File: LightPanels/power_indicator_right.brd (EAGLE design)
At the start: 47.5 x 48 mm, 22 parts

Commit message: Latest light panel pcb files
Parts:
- moved U$7 36.3 mm to (9.05, 9.37), turned to 180 degrees
- moved C7 35.9 mm to (8.89, 13.0), turned to 0 degrees
- moved U$1 35.8 mm to (24.1, 37.1), turned to 270 degrees
- moved C1 34.7 mm to (21.0, 34.6), turned to 270 degrees
- moved U$2 25.6 mm to (22.2, 27.5), turned to 270 degrees
- moved PAD8 23.3 mm to (19.1, 20.3), turned to 90 degrees
- moved C2 23.0 mm to (20.6, 22.9), turned to 270 degrees
- moved PAD6 22.7 mm to (19.1, 8.89), turned to 90 degrees
- moved C6 22.1 mm to (18.7, 15.2), turned to 0 degrees
- moved PAD7 21.8 mm to (19.1, 16.5), turned to 90 degrees
- moved U$6 21.8 mm to (19.1, 11.7), turned to 180 degrees
- moved PAD5 21.6 mm to (19.1, 12.7), turned to 90 degrees
- moved C3 17.7 mm to (24.1, 21.3), turned to 90 degrees
- moved U$3 14.1 mm to (27.5, 21.3), turned to 270 degrees
- moved PAD4 12.7 mm to (27.9, 20.3), turned to 90 degrees
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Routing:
- net GND: track 36.5 -> 41.1 mm
- net +5V: track 6.69 -> 7.96 mm, vias 1 -> 2
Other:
- board size 47.5 x 48 mm -> 48 x 47.5 mm

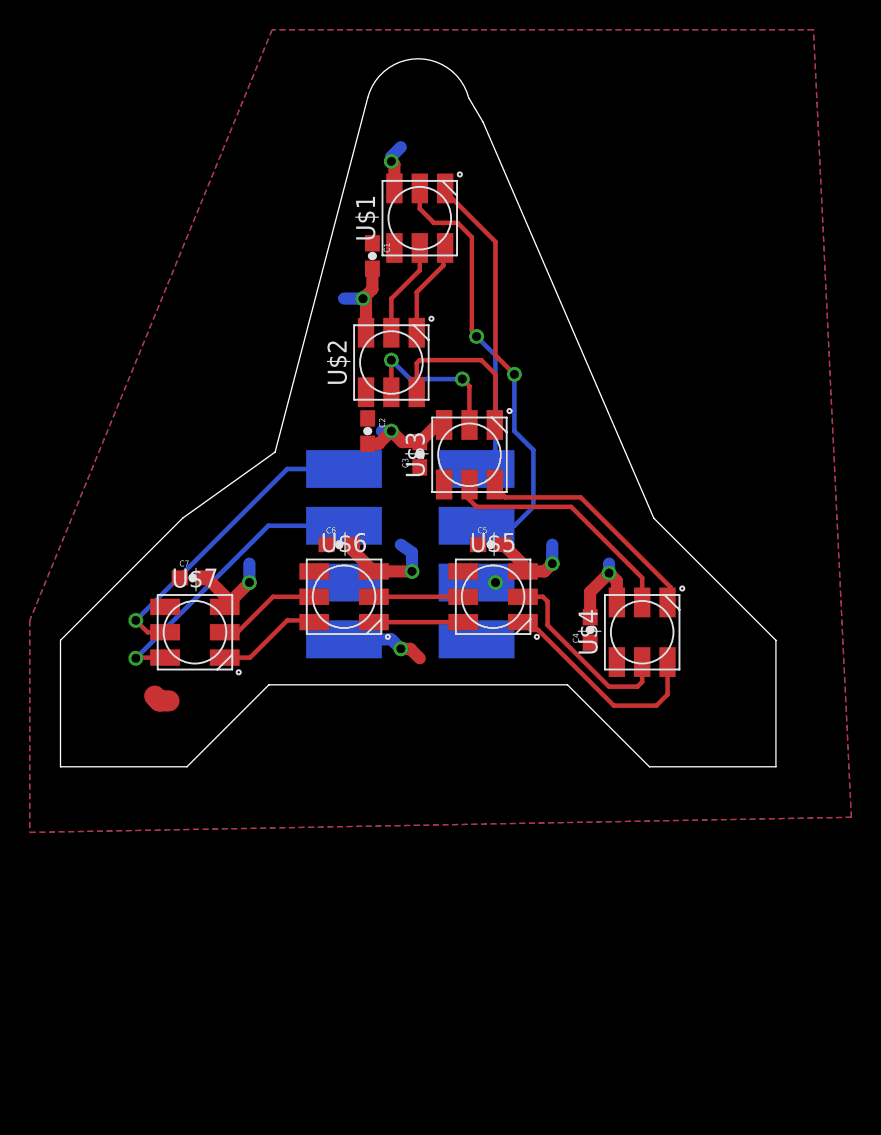
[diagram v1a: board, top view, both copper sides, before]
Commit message: Power indicators more or less done
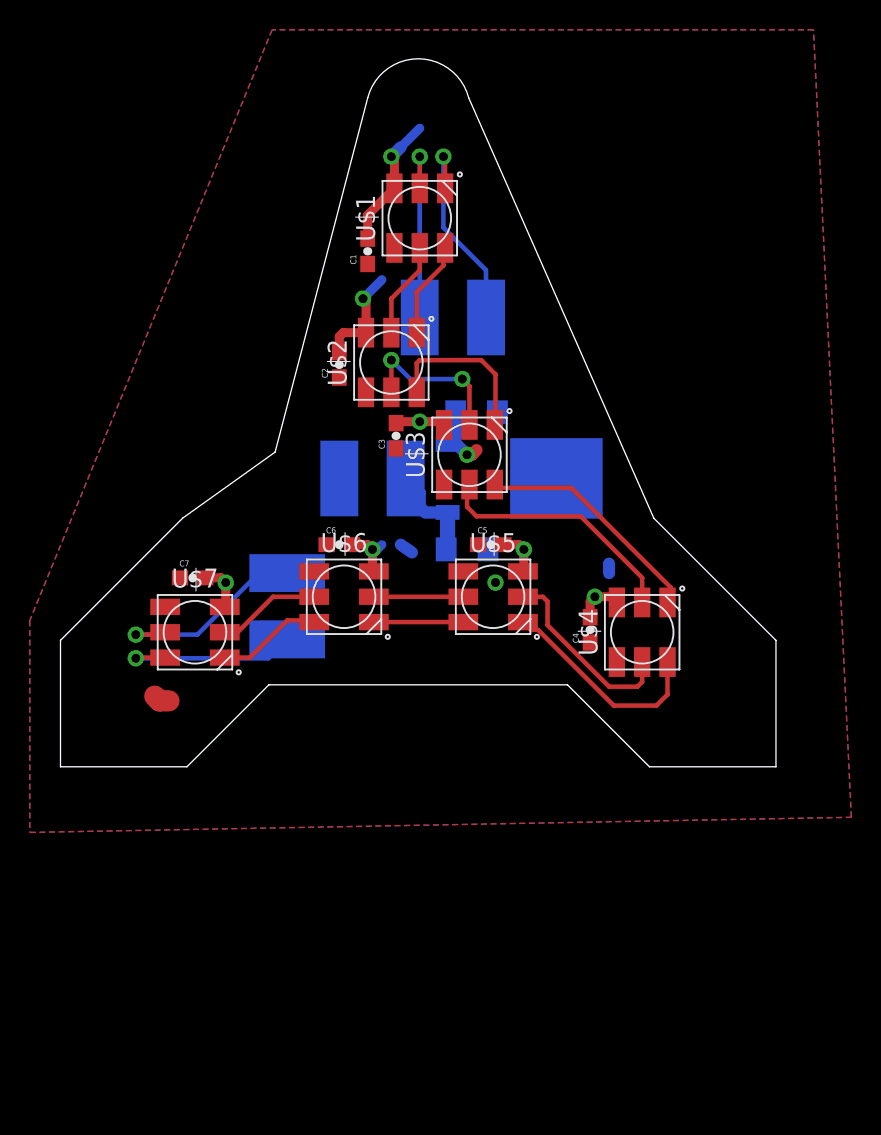
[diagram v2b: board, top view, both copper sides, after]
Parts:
- removed PAD1, PAD2, PAD3, PAD4, PAD5, PAD6, PAD7, PAD8: WIREPADSMD2,54-5,08, wirepad:SMD2,54-5,08
- added +12V, CI, CO, DI, DO, GND: WIREPADSMD2,54-5,08, wirepad:SMD2,54-5,08
- added C8, C9: 10uF, SparkFun-Retired:EIA3216
- added IC1: 7805DT, linear:TO252
- moved C2 4.84 mm to (18.7, 27.3), turned to 90 degrees
- moved C3 2.03 mm to (22.5, 22.5)
- moved C1 0.45 mm to (20.6, 34.9), turned to 90 degrees
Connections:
- new net +12V: +12V.1, C9.A, IC1.1
- net +5V: now also C8.A, IC1.2; no longer PAD2.1, PAD6.1
- net GND: now also C8.C, C9.C, GND.1; no longer PAD1.1, PAD5.1
- net N$13: now also CO.1; no longer PAD8.1
- net N$14: now also DO.1; no longer PAD7.1
- net N$15: now also DI.1; no longer PAD3.1
- net N$16: now also CI.1; no longer PAD4.1
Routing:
- net N$15: track 28.2 -> 14.4 mm
- net N$16: track 22.4 -> 12.9 mm
- net N$14: track 19.6 -> 12.7 mm
- net +12V: track 0.00 -> 6.84 mm
- net GND: track 41.1 -> 35.0 mm
- net N$13: track 20.5 -> 14.4 mm
- net +5V: track 7.96 -> 5.83 mm
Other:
- outline, holes or cut-outs redrawn

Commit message: Clean up light panels. Remvoe names/values
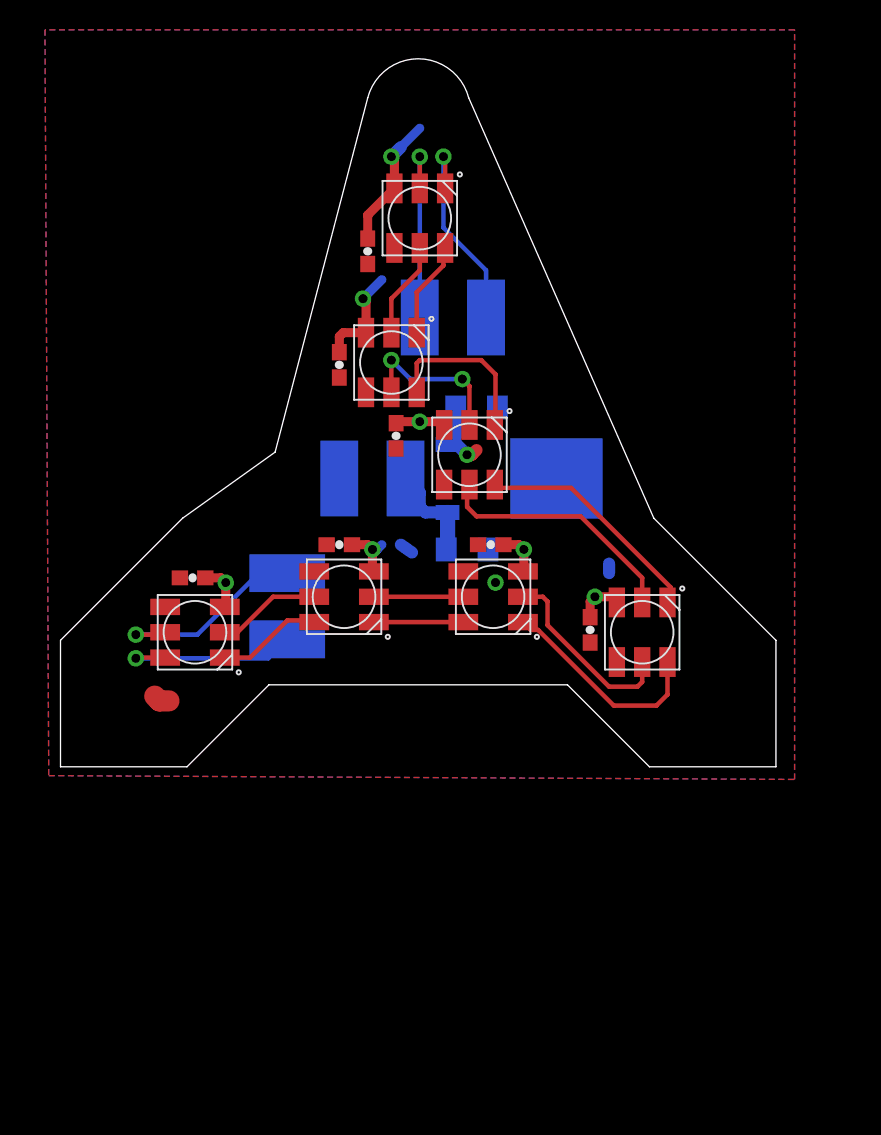
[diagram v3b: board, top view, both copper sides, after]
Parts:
- moved C8 0.32 mm to (27.9, 24.4)
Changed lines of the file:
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@@
 </autorouter>
 <elements>
-<element name="C1" library="SparkFun-Capacitors" package="0603-CAP" value="0.1uF" x="20.6375" y="34.925" rot="R90">
+<element name="C1" library="SparkFun-Capacitors" package="0603-CAP" value="0.1uF" x="20.6375" y="34.925" smashed="yes" rot="R90">
 <attribute name="PROD_ID" value="CAP-08390" x="20.6375" y="34.925" size="1.778" layer="27" rot="R90" display="off"/>
 </element>
-<element name="C2" library="SparkFun-Capacitors" package="0603-CAP" value="0.1uF" x="18.7325" y="27.305" rot="R90">
+<element name="C2" library="SparkFun-Capacitors" package="0603-CAP" value="0.1uF" x="18.7325" y="27.305" smashed="yes" rot="R90">
 <attribute name="PROD_ID" value="CAP-08390" x="18.7325" y="27.305" size="1.778" layer="27" rot="R90" display="off"/>
 </element>
-<element name="C3" library="SparkFun-Capacitors" package="0603-CAP" value="0.1uF" x="22.5425" y="22.5425" rot="R90">
+<element name="C3" library="SparkFun-Capacitors" package="0603-CAP" value="0.1uF" x="22.5425" y="22.5425" smashed="yes" rot="R90">
 <attribute name="PROD_ID" value="CAP-08390" x="22.5425" y="22.5425" size="1.778" layer="27" rot="R90" display="off"/>
 </element>
-<element name="C4" library="SparkFun-Capacitors" package="0603-CAP" value="0.1uF" x="35.56" y="9.525" rot="R90">
+<element name="C4" library="SparkFun-Capacitors" package="0603-CAP" value="0.1uF" x="35.56" y="9.525" smashed="yes" rot="R90">
 <attribute name="PROD_ID" value="CAP-08390" x="35.56" y="9.525" size="1.778" layer="27" rot="R90" display="off"/>
 </element>
-<element name="C5" library="SparkFun-Capacitors" package="0603-CAP" value="0.1uF" x="28.8925" y="15.24">
+<element name="C5" library="SparkFun-Capacitors" package="0603-CAP" value="0.1uF" x="28.8925" y="15.24" smashed="yes">
 <attribute name="PROD_ID" value="CAP-08390" x="28.8925" y="15.24" size="1.778" layer="27" display="off"/>
 </element>
-<element name="C6" library="SparkFun-Capacitors" package="0603-CAP" value="0.1uF" x="18.7325" y="15.24">
+<element name="C6" library="SparkFun-Capacitors" package="0603-CAP" value="0.1uF" x="18.7325" y="15.24" smashed="yes">
 <attribute name="PROD_ID" value="CAP-08390" x="18.7325" y="15.24" size="1.778" layer="27" display="off"/>
 </element>
-<element name="C7" library="SparkFun-Capacitors" package="0603-CAP" value="0.1uF" x="8.89" y="13.0175">
+<element name="C7" library="SparkFun-Capacitors" package="0603-CAP" value="0.1uF" x="8.89" y="13.0175" smashed="yes">
 <attribute name="PROD_ID" value="CAP-08390" x="8.89" y="13.0175" size="1.778" layer="27" display="off"/>
 </element>
-<element name="U$1" library="jos-ph" package="APA102_5050" value="APA1025050" x="24.13" y="37.1475" rot="R270"/>
-<element name="U$2" library="jos-ph" package="APA102_5050" value="APA1025050" x="22.225" y="27.46375" rot="R270"/>
-<element name="U$3" library="jos-ph" package="APA102_5050" value="APA1025050" x="27.46375" y="21.2725" rot="R270"/>
-<element name="U$4" library="jos-ph" package="APA102_5050" value="APA1025050" x="39.0525" y="9.36625" rot="R270"/>
-<element name="U$5" library="jos-ph" package="APA102_5050" value="APA1025050" x="29.05125" y="11.7475" rot="R180"/>
-<element name="U$6" library="jos-ph" package="APA102_5050" value="APA1025050" x="19.05" y="11.7475" rot="R180"/>
-<element name="U$7" library="jos-ph" package="APA102_5050" value="APA1025050" x="9.04875" y="9.36625" rot="R180"/>
-<element name="GND" library="wirepad" package="SMD2,54-5,08" value="WIREPADSMD2,54-5,08" x="18.7325" y="19.685" rot="MR180"/>
-<element name="+12V" library="wirepad" package="SMD2,54-5,08" value="WIREPADSMD2,54-5,08" x="23.1775" y="19.685" rot="MR180"/>
-<element name="DI" library="wirepad" package="SMD2,54-5,08" value="WIREPADSMD2,54-5,08" x="28.575" y="30.48" rot="MR0"/>
-<element name="CI" library="wirepad" package="SMD2,54-5,08" value="WIREPADSMD2,54-5,08" x="24.13" y="30.48" rot="MR0"/>
-<element name="DO" library="wirepad" package="SMD2,54-5,08" value="WIREPADSMD2,54-5,08" x="15.24" y="8.89" rot="MR270"/>
-<element name="CO" library="wirepad" package="SMD2,54-5,08" value="WIREPADSMD2,54-5,08" x="15.24" y="13.335" rot="MR270"/>
-<element name="IC1" library="linear" package="TO252" value="7805DT" x="30.7975" y="19.685" rot="MR90"/>
-<element name="C8" library="SparkFun-Retired" package="EIA3216" value="10uF" x="27.94" y="24.13" rot="MR0">
-<attribute name="PROD_ID" value="CAP-00811" x="27.94" y="24.13" size="1.778" layer="28" rot="MR0" display="off"/>
+<element name="U$1" library="jos-ph" package="APA102_5050" value="APA1025050" x="24.13" y="37.1475" smashed="yes" rot="R270"/>
+<element name="U$2" library="jos-ph" package="APA102_5050" value="APA1025050" x="22.225" y="27.46375" smashed="yes" rot="R270"/>
+<element name="U$3" library="jos-ph" package="APA102_5050" value="APA1025050" x="27.46375" y="21.2725" smashed="yes" rot="R270"/>
+<element name="U$4" library="jos-ph" package="APA102_5050" value="APA1025050" x="39.0525" y="9.36625" smashed="yes" rot="R270"/>
+<element name="U$5" library="jos-ph" package="APA102_5050" value="APA1025050" x="29.05125" y="11.7475" smashed="yes" rot="R180"/>
+<element name="U$6" library="jos-ph" package="APA102_5050" value="APA1025050" x="19.05" y="11.7475" smashed="yes" rot="R180"/>
+<element name="U$7" library="jos-ph" package="APA102_5050" value="APA1025050" x="9.04875" y="9.36625" smashed="yes" rot="R180"/>
+<element name="GND" library="wirepad" package="SMD2,54-5,08" value="WIREPADSMD2,54-5,08" x="18.7325" y="19.685" smashed="yes" rot="MR180">
+<attribute name="NAME" x="17.2325" y="22.185" size="1.27" layer="26" rot="MR270"/>
 </element>
-<element name="C9" library="SparkFun-Retired" package="EIA3216" value="10uF" x="27.305" y="14.9225" rot="MR0">
+<element name="+12V" library="wirepad" package="SMD2,54-5,08" value="WIREPADSMD2,54-5,08" x="23.1775" y="19.685" smashed="yes" rot="MR180">
+<attribute name="NAME" x="21.6775" y="22.185" size="1.27" layer="26" rot="MR270"/>
+</element>
+<element name="DI" library="wirepad" package="SMD2,54-5,08" value="WIREPADSMD2,54-5,08" x="28.575" y="30.48" smashed="yes" rot="MR0">
+<attribute name="NAME" x="30.075" y="27.98" size="1.27" layer="26" rot="MR90"/>
+</element>
+<element name="CI" library="wirepad" package="SMD2,54-5,08" value="WIREPADSMD2,54-5,08" x="24.13" y="30.48" smashed="yes" rot="MR0">
+<attribute name="NAME" x="25.63" y="27.98" size="1.27" layer="26" rot="MR90"/>
+</element>
+<element name="DO" library="wirepad" package="SMD2,54-5,08" value="WIREPADSMD2,54-5,08" x="15.24" y="8.89" smashed="yes" rot="MR270">
+<attribute name="NAME" x="17.74" y="10.39" size="1.27" layer="26" rot="MR0"/>
+</element>
+<element name="CO" library="wirepad" package="SMD2,54-5,08" value="WIREPADSMD2,54-5,08" x="15.24" y="13.335" smashed="yes" rot="MR270">
+<attribute name="NAME" x="17.74" y="14.835" size="1.27" layer="26" rot="MR0"/>
+</element>
+<element name="IC1" library="linear" package="TO252" value="7805DT" x="30.7975" y="19.685" smashed="yes" rot="MR90"/>
+<element name="C8" library="SparkFun-Retired" package="EIA3216" value="10uF" x="27.94" y="24.4475" smashed="yes" rot="MR0">
+<attribute name="PROD_ID" value="CAP-00811" x="27.94" y="24.4475" size="1.778" layer="28" rot="MR0" display="off"/>
+</element>
+<element name="C9" library="SparkFun-Retired" package="EIA3216" value="10uF" x="27.305" y="14.9225" smashed="yes" rot="MR0">
 <attribute name="PROD_ID" value="CAP-00811" x="27.305" y="14.9225" size="1.778" layer="28" rot="MR0" display="off"/>
 </element>
@@
 <contactref element="C7" pad="2"/>
 <polygon width="0.3048" layer="16">
-<vertex x="50.546" y="49.784"/>
-<vertex x="14.224" y="49.784"/>
-<vertex x="-2.032" y="10.16"/>
-<vertex x="-2.032" y="-4.064"/>
-<vertex x="53.086" y="-3.048"/>
+<vertex x="49.276" y="49.784"/>
+<vertex x="-1.016" y="49.784"/>
+<vertex x="-0.762" y="-0.254"/>
+<vertex x="49.276" y="-0.508"/>
 </polygon>
 <wire x1="22.225" y1="41.275" x2="22.86" y2="41.91" width="0.8128" layer="16"/>
@@
 <contactref element="U$7" pad="1"/>
 <polygon width="0.3048" layer="1">
-<vertex x="50.546" y="49.784"/>
-<vertex x="14.224" y="49.784"/>
-<vertex x="-2.032" y="10.16"/>
-<vertex x="-2.032" y="-4.064"/>
-<vertex x="53.086" y="-3.048"/>
+<vertex x="49.276" y="49.784"/>
+<vertex x="-1.016" y="49.784"/>
+<vertex x="-0.762" y="-0.254"/>
+<vertex x="49.276" y="-0.508"/>
 </polygon>
 <wire x1="7.3025" y1="4.7625" x2="6.6675" y2="4.7625" width="1.4224" layer="1"/>
@@
 <contactref element="IC1" pad="2"/>
 <contactref element="C8" pad="A"/>
-<wire x1="26.54" y1="24.13" x2="26.54" y2="22.5075" width="0.8128" layer="16"/>
+<wire x1="26.54" y1="24.4475" x2="26.54" y2="22.5075" width="0.8128" layer="16"/>
 <wire x1="26.54" y1="22.5075" x2="25.9975" y2="21.965" width="0.8128" layer="16"/>
 <wire x1="25.9975" y1="21.965" x2="26.6125" y2="21.965" width="0.8128" layer="16"/>
